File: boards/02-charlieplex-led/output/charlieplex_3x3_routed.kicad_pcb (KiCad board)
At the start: 2 copper layers, 50 x 55 mm, 14 parts, among them U1 MCU

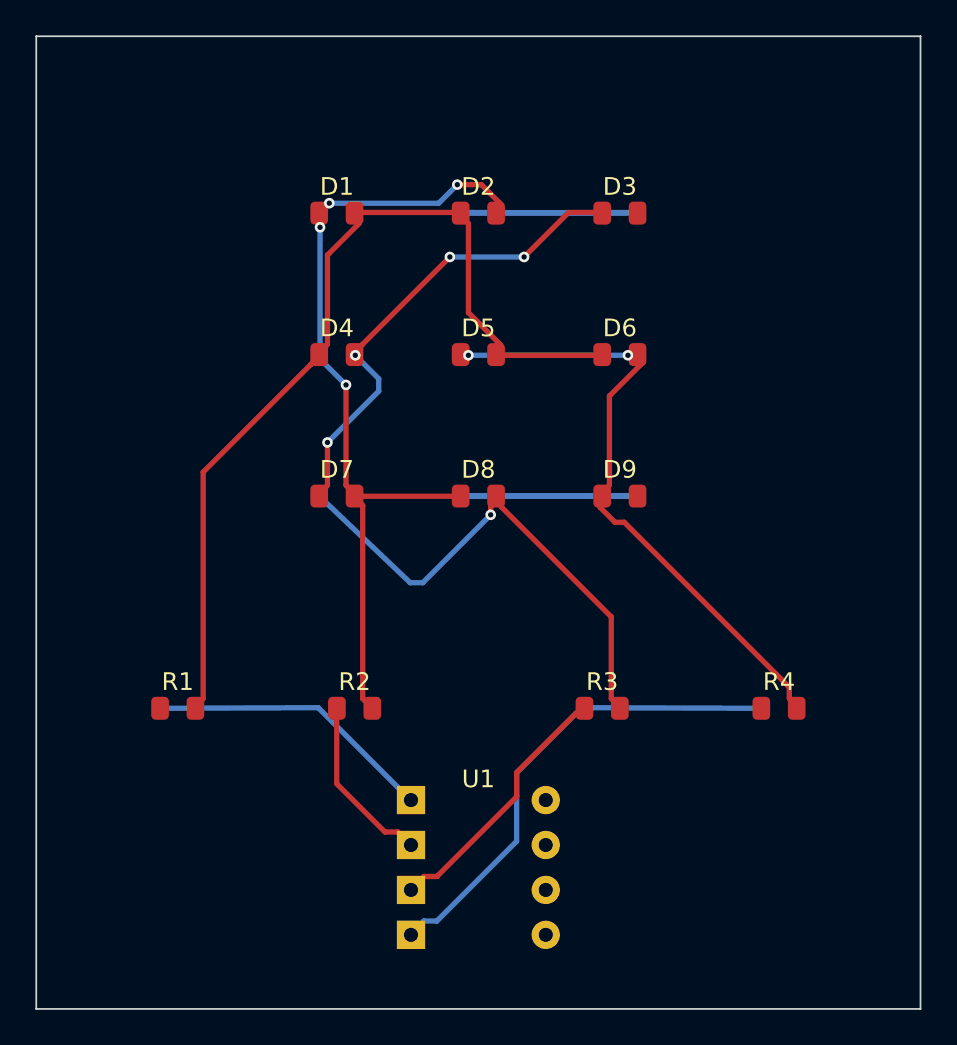
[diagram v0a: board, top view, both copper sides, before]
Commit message: wip: regenerate boards 01/02 at KiCad 10 format + bump roundtrip guard to 10.0
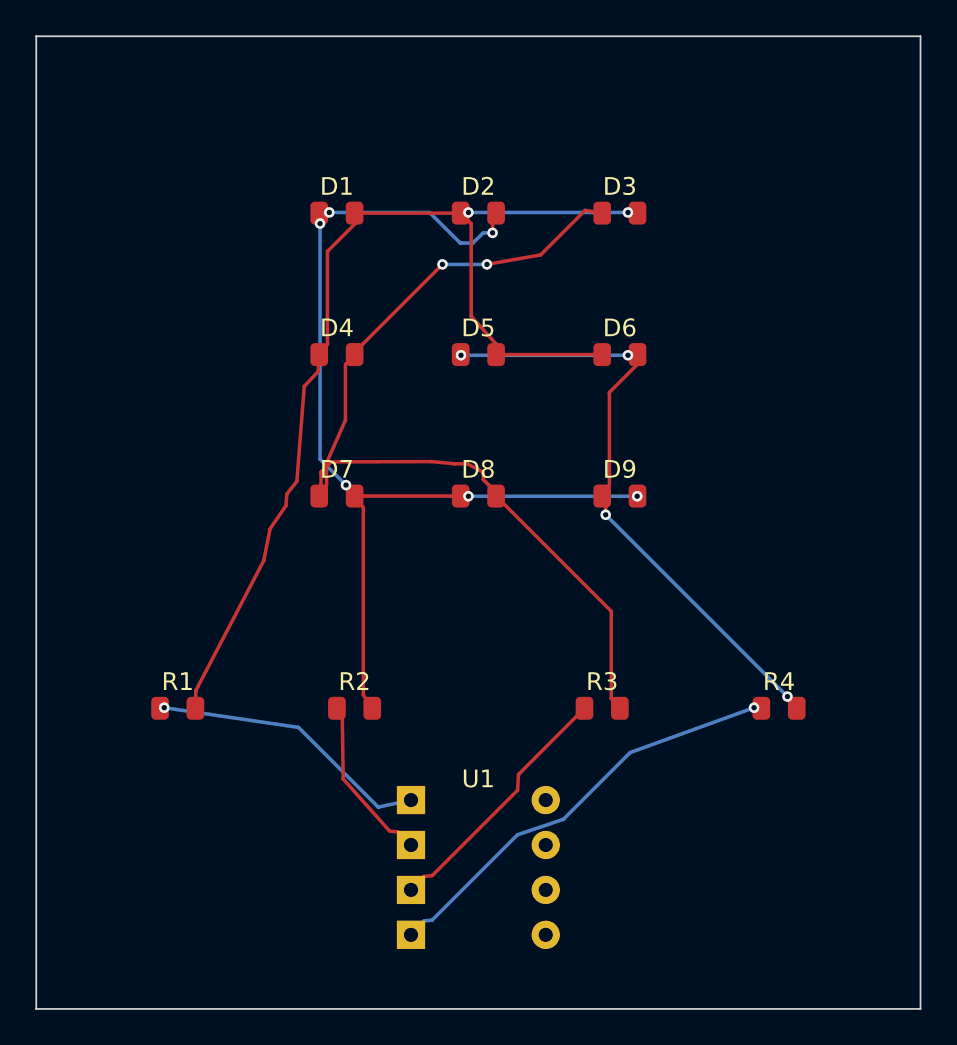
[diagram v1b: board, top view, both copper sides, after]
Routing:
- net NODE_A: track 72.1 -> 61.4 mm, vias 0 -> 2
- net NODE_B: track 66.5 -> 57.0 mm, vias 4 -> 6
- net NODE_C: track 56.5 -> 53.2 mm, vias 5 -> 2
- net LINE_D: track 27.4 -> 24.3 mm, vias 0 -> 1
- net NODE_D: track 35.8 -> 35.3 mm, vias 2 -> 4
- net LINE_A: track 16.3 -> 16.2 mm, vias 0 -> 1
